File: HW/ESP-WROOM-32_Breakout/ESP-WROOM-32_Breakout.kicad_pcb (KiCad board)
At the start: 2 copper layers, 33 x 48 mm, 10 parts, among them P1 CONN_01X06, P2 CONN_01X18, P3 CONN_01X18, U1 ESP32-WROOM

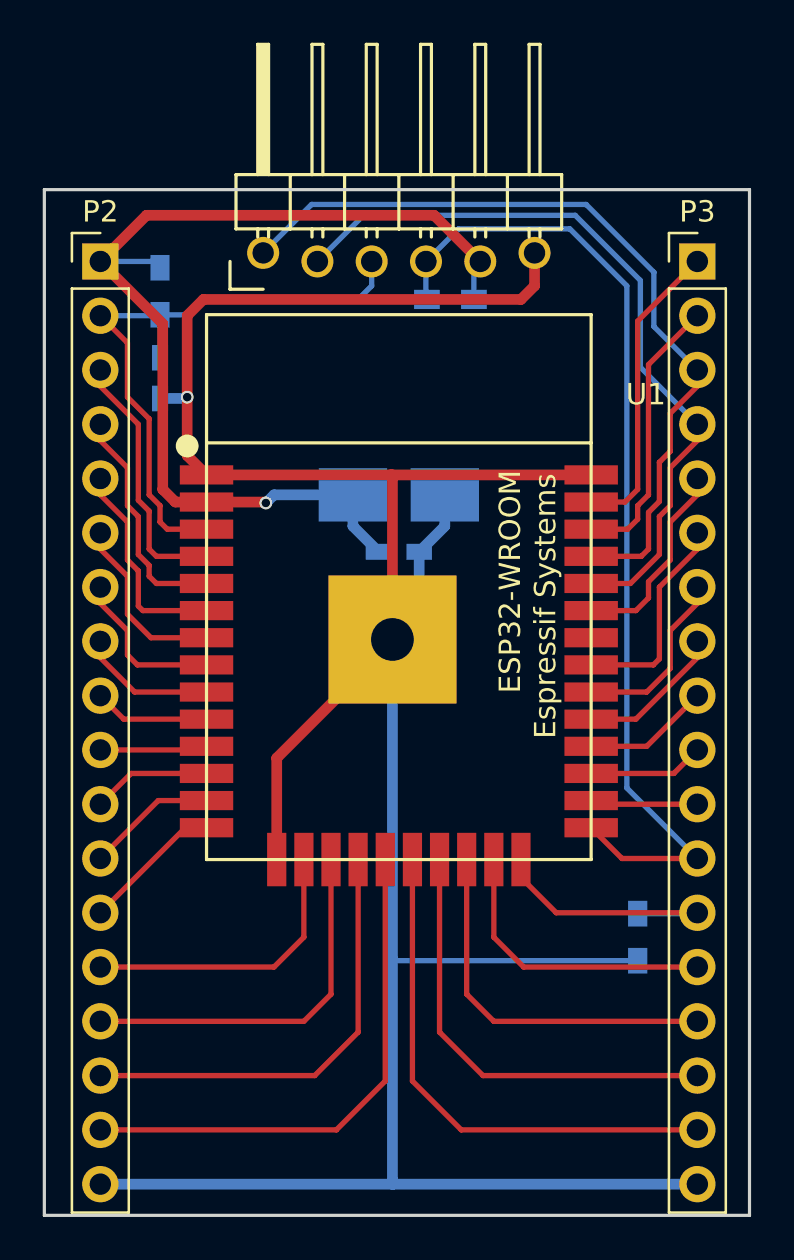
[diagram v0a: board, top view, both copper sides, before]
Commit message: Modify ESP-32 Breakout
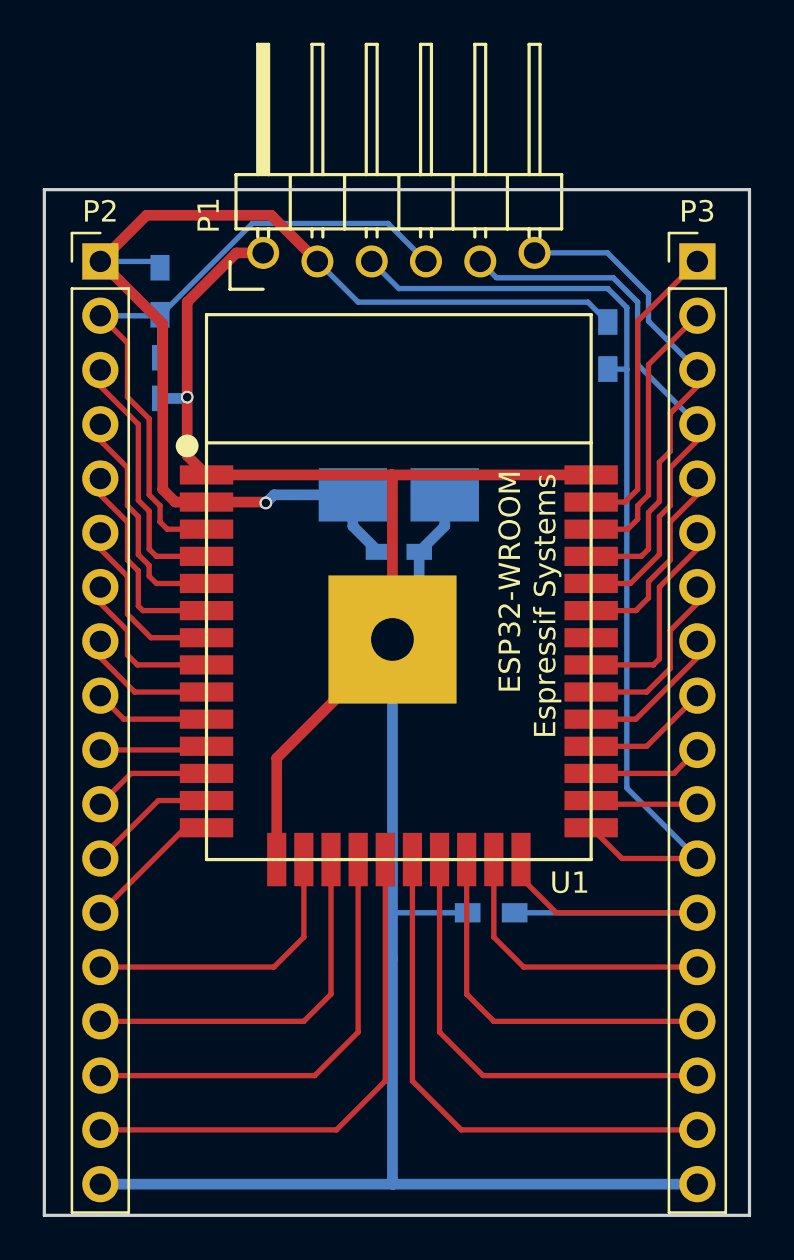
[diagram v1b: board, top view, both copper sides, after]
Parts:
- P1: value CONN_01X06 -> ISP
- moved R3 7.68 mm to (158.4, 90.3), turned to 270 degrees
- moved R2 6.95 mm to (152.9, 116.8), turned to 180 degrees
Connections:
- P1 pad 1: TXD -> GND
- P1 pad 2: RXD -> VCC
- P1 pad 3: ~RST -> ~FLASH
- P1 pad 4: ~FLASH -> ~RST
- P1 pad 5: VCC -> RXD
- P1 pad 6: GND -> TXD
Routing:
- net GND: track 139.0 -> 117.7 mm
- net TXD: track 38.1 -> 22.8 mm
- net RXD: track 35.7 -> 25.6 mm
- net Net-(P3-Pad13): track 12.6 -> 18.3 mm
- net VCC: track 48.7 -> 54.0 mm
- net ~RST: track 29.6 -> 32.9 mm
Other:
- board text added: "Designed by SUF"
- board text added: "ESP32 Development Board"
- board text added: "FLASH"
- board text added: "GND"
- board text added: "RESET"
- board text added: "RXD"
- board text added: "TXD"
- board text added: "VCC"
